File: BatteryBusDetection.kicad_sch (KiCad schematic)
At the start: 12 parts, among them U1 S-8209AAA-T8T1U, U2 S-8209AAA-T8T1U

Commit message: Refactored schematics and silkscreen
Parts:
- C1, C2, C3, C4: footprint (none) -> Capacitor_SMD:C_0603_1608Metric
- R1, R2, R4, R5, R6, R7: footprint (none) -> Resistor_SMD:R_0603_1608Metric
- U1, U2: footprint TSSOP8-E-PKG_FT008-A-P-SD-1.2_ABL -> Battery-Board:TSSOP8-E-PKG_FT008-A-P-SD-1.2_ABL
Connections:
- net CHARGE_ENABLE renamed CHARGE_EN
- net DISCHARGE_ENABLE renamed DISCHARGE_EN
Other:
- note added: "delay = 10MOhms * C_cdt"
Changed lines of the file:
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@@
 		)
 	)
-	(hierarchical_label "CHARGE_ENABLE"
-		(shape output)
-		(at 237.49 81.28 0)
-		(fields_autoplaced yes)
+	(text "delay = 10MOhms * C_cdt"
+		(exclude_from_sim no)
+		(at 116.078 132.588 0)
 		(effects
 			(font
 				(size 1.27 1.27)
 			)
+		)
+	)
+	(hierarchical_label "CHARGE_EN"
+		(shape output)
+		(at 237.49 81.28 0)
+		(fields_autoplaced yes)
+		(effects
+			(font
+				(size 1.27 1.27)
+			)
 			(justify left)
 		)
@@
 		)
 	)
-	(hierarchical_label "DISCHARGE_ENABLE"
+	(hierarchical_label "DISCHARGE_EN"
 		(shape output)
 		(at 237.49 83.82 0)
@@
 			)
 		)
-		(property "Footprint" ""
+		(property "Footprint" "Resistor_SMD:R_0603_1608Metric"
 			(at 161.29 102.87 0)
 			(effects
@@
 			)
 		)
-		(property "Footprint" ""
+		(property "Footprint" "Resistor_SMD:R_0603_1608Metric"
 			(at 102.87 105.41 0)
 			(effects
@@
 			)
 		)
-		(property "Footprint" ""
+		(property "Footprint" "Capacitor_SMD:C_0603_1608Metric"
 			(at 102.87 124.46 0)
 			(effects
@@
 			)
 		)
-		(property "Footprint" ""
+		(property "Footprint" "Resistor_SMD:R_0603_1608Metric"
 			(at 92.71 124.46 0)
 			(effects
@@
 			)
 		)
-		(property "Footprint" "TSSOP8-E-PKG_FT008-A-P-SD-1.2_ABL"
+		(property "Footprint" "Battery-Board:TSSOP8-E-PKG_FT008-A-P-SD-1.2_ABL"
 			(at 116.84 111.76 0)
 			(effects
@@
 			)
 		)
-		(property "Footprint" ""
+		(property "Footprint" "Capacitor_SMD:C_0603_1608Metric"
 			(at 182.88 91.44 0)
 			(effects
@@
 			)
 		)
-		(property "Footprint" ""
+		(property "Footprint" "Resistor_SMD:R_0603_1608Metric"
 			(at 171.45 69.85 0)
 			(effects
@@
 			)
 		)
-		(property "Footprint" ""
+		(property "Footprint" "Capacitor_SMD:C_0603_1608Metric"
 			(at 171.45 91.44 0)
 			(effects
@@
 			)
 		)
-		(property "Footprint" ""
+		(property "Footprint" "Capacitor_SMD:C_0603_1608Metric"
 			(at 114.3 124.46 0)
 			(effects
@@
 			)
 		)
-		(property "Footprint" ""
+		(property "Footprint" "Resistor_SMD:R_0603_1608Metric"
 			(at 167.64 111.76 0)
 			(effects
@@
 			)
 		)
-		(property "Footprint" "TSSOP8-E-PKG_FT008-A-P-SD-1.2_ABL"
+		(property "Footprint" "Battery-Board:TSSOP8-E-PKG_FT008-A-P-SD-1.2_ABL"
 			(at 185.42 78.74 0)
 			(effects
@@
 			)
 		)
-		(property "Footprint" ""
+		(property "Footprint" "Resistor_SMD:R_0603_1608Metric"
 			(at 83.82 124.46 0)
 			(effects

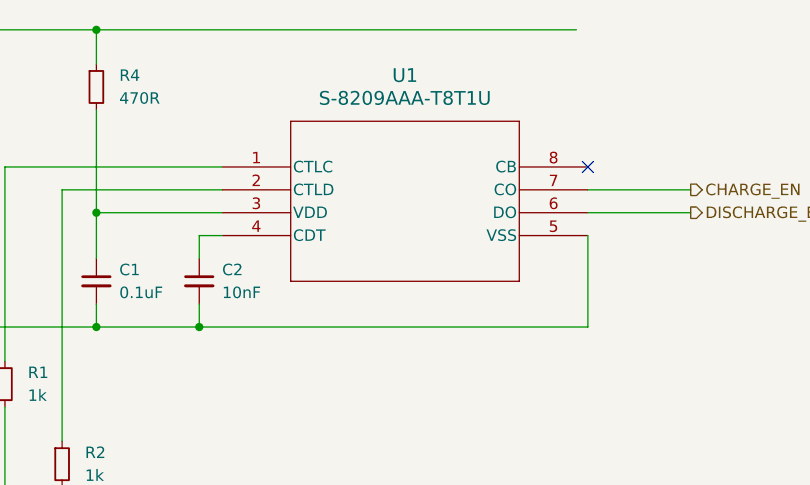
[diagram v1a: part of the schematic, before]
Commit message: Changes for lib refactor
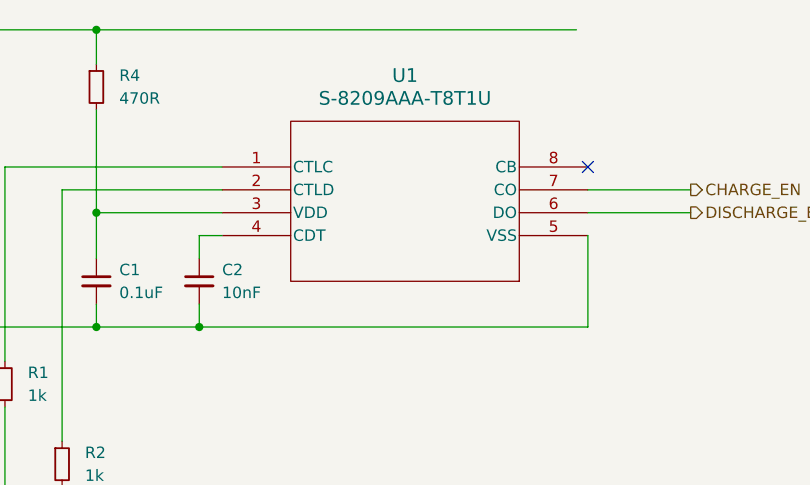
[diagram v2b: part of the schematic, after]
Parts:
- U1, U2: footprint Battery-Board:TSSOP8-E-PKG_FT008-A-P-SD-1.2_ABL -> Argus-IC:TSSOP8-E-PKG_FT008-A-P-SD-1.2_ABL; symbol Battery-Board:S-8209AAA-T8T1U -> Argus-IC:S-8209AAA-T8T1U
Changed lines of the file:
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@@
 	)
 	(symbol
-		(lib_name "S-8209AAA-T8T1U_1")
-		(lib_id "Battery-Board:S-8209AAA-T8T1U")
+		(lib_id "Argus-IC:S-8209AAA-T8T1U")
 		(at 116.84 111.76 0)
 		(unit 1)
@@
 			)
 		)
-		(property "Footprint" "Battery-Board:TSSOP8-E-PKG_FT008-A-P-SD-1.2_ABL"
+		(property "Footprint" "Argus-IC:TSSOP8-E-PKG_FT008-A-P-SD-1.2_ABL"
 			(at 116.84 111.76 0)
 			(effects
@@
 	)
 	(symbol
-		(lib_id "Battery-Board:S-8209AAA-T8T1U")
+		(lib_id "Argus-IC:S-8209AAA-T8T1U")
 		(at 185.42 78.74 0)
 		(unit 1)
@@
 			)
 		)
-		(property "Footprint" "Battery-Board:TSSOP8-E-PKG_FT008-A-P-SD-1.2_ABL"
+		(property "Footprint" "Argus-IC:TSSOP8-E-PKG_FT008-A-P-SD-1.2_ABL"
 			(at 185.42 78.74 0)
 			(effects

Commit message: Fixes from feedback
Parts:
- U1, U2: footprint Argus-IC:TSSOP8-E-PKG_FT008-A-P-SD-1.2_ABL -> TSSOP8-E-PKG_FT008-A-P-SD-1.2_ABL
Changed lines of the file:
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@@
 			)
 		)
-		(property "Footprint" "Argus-IC:TSSOP8-E-PKG_FT008-A-P-SD-1.2_ABL"
+		(property "Footprint" "TSSOP8-E-PKG_FT008-A-P-SD-1.2_ABL"
 			(at 116.84 111.76 0)
 			(effects
@@
 			)
 		)
-		(property "Footprint" "Argus-IC:TSSOP8-E-PKG_FT008-A-P-SD-1.2_ABL"
+		(property "Footprint" "TSSOP8-E-PKG_FT008-A-P-SD-1.2_ABL"
 			(at 185.42 78.74 0)
 			(effects

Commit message: v2.1 (v3?) Partial Updates
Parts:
- U1: renamed from U2; footprint TSSOP8-E-PKG_FT008-A-P-SD-1.2_ABL -> Argus-IC:TSSOP8-E-PKG_FT008-A-P-SD-1.2_ABL
- U2: renamed from U1; footprint TSSOP8-E-PKG_FT008-A-P-SD-1.2_ABL -> Argus-IC:TSSOP8-E-PKG_FT008-A-P-SD-1.2_ABL
- renumbered C3 to C1, C4 to C2, C1 to C3, C2 to C4, R7 to R1, R6 to R2, R5 to R3, R1 to R4, R2 to R5, R4 to R6
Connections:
- net BATT0 renamed BATT_N
- net BATT1 renamed BATT_M
- net BATT2 renamed BATT_P
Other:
- note added: "Battery protection design derived from Portland State University's Open-Source OreSat project"
- note added: "S-8209A has a Vov = 4.100V (release = 4.000V) and a Vuv = 2.500V (release = 2.700V)"
- note added: "t_D = 10.0 MΩ typ. × C_CDT [μF] t_D = 0.1s"
- note removed: "delay = 10MOhms * C_cdt"
- company: (none) -> Carnegie Mellon University
- title: (none) -> Argus Batteryboard
- moved on the sheet: C1, C2, C3, C4, R1, R2, R3, R4, R5, R6, U1, U2

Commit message: v3.1 Updates
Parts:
- C1, C3: value 0.1uF -> 100n
- C2, C4: value 10nF -> 10n
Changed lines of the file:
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@@
 		(dnp no)
 		(property "Reference" "C1"
-			(at 88.646 124.714 0)
-			(effects
-				(font
-					(size 1.27 1.27)
-				)
-				(justify left)
-			)
-		)
-		(property "Value" "0.1uF"
-			(at 88.646 126.746 0)
+			(at 88.392 124.714 0)
+			(effects
+				(font
+					(size 1.27 1.27)
+				)
+				(justify left)
+			)
+		)
+		(property "Value" "100n"
+			(at 88.392 126.746 0)
 			(effects
 				(font
@@
 		(dnp no)
 		(property "Reference" "C4"
-			(at 167.386 91.694 0)
-			(effects
-				(font
-					(size 1.27 1.27)
-				)
-				(justify left)
-			)
-		)
-		(property "Value" "10nF"
-			(at 167.386 93.726 0)
+			(at 167.132 91.694 0)
+			(effects
+				(font
+					(size 1.27 1.27)
+				)
+				(justify left)
+			)
+		)
+		(property "Value" "10n"
+			(at 167.132 93.726 0)
 			(effects
 				(font
@@
 		(dnp no)
 		(property "Reference" "C3"
-			(at 157.226 91.694 0)
-			(effects
-				(font
-					(size 1.27 1.27)
-				)
-				(justify left)
-			)
-		)
-		(property "Value" "0.1uF"
-			(at 157.226 93.726 0)
+			(at 156.972 91.694 0)
+			(effects
+				(font
+					(size 1.27 1.27)
+				)
+				(justify left)
+			)
+		)
+		(property "Value" "100n"
+			(at 156.972 93.726 0)
 			(effects
 				(font
@@
 		(dnp no)
 		(property "Reference" "C2"
-			(at 98.806 124.714 0)
-			(effects
-				(font
-					(size 1.27 1.27)
-				)
-				(justify left)
-			)
-		)
-		(property "Value" "10nF"
-			(at 98.806 126.746 0)
-			(effects
-				(font
+			(at 98.552 124.714 0)
+			(effects
+				(font
+					(size 1.27 1.27)
+				)
+				(justify left)
+			)
+		)
+		(property "Value" "10n"
+			(at 98.552 126.746 0)
+			(effects
+				(font

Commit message: Idk some changes
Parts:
- C1, C3: MPN (none) -> C307348
- C2, C4: MPN (none) -> C161232
- R1, R2, R4, R5: MPN (none) -> C2484712
- R3, R6: MPN (none) -> C844564
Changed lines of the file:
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@@
+			)
+		)
+		(property "MPN" "C2484712"
+			(at 142.24 92.71 0)
+			(effects
+				(font
+					(size 1.27 1.27)
+				)
+				(hide yes)
 			)
 		)
@@
 			)
 		)
+		(property "MPN" "C844564"
+			(at 86.36 106.68 0)
+			(effects
+				(font
+					(size 1.27 1.27)
+				)
+				(hide yes)
+			)
+		)
 		(pin "2"
 		)
@@
 			)
 		)
+		(property "MPN" "C307348"
+			(at 86.36 125.73 0)
+			(effects
+				(font
+					(size 1.27 1.27)
+				)
+				(hide yes)
+			)
+		)
 		(pin "1"
 		)
@@
 			)
 		)
+		(property "MPN" "C2484712"
+			(at 80.01 125.73 0)
+			(effects
+				(font
+					(size 1.27 1.27)
+				)
+				(hide yes)
+			)
+		)
 		(pin "2"
 		)
@@
 			)
 		)
+		(property "MPN" "C161232"
+			(at 165.1 92.71 0)
+			(effects
+				(font
+					(size 1.27 1.27)
+				)
+				(hide yes)
+			)
+		)
 		(pin "1"
 		)
@@
 			)
 		)
+		(property "MPN" "C844564"
+			(at 154.94 71.12 0)
+			(effects
+				(font
+					(size 1.27 1.27)
+				)
+				(hide yes)
+			)
+		)
 		(pin "2"
 		)
@@
 			)
 		)
+		(property "MPN" "C307348"
+			(at 154.94 92.71 0)
+			(effects
+				(font
+					(size 1.27 1.27)
+				)
+				(hide yes)
+			)
+		)
 		(pin "1"
 		)
@@
 			)
 		)
+		(property "MPN" "C161232"
+			(at 96.52 125.73 0)
+			(effects
+				(font
+					(size 1.27 1.27)
+				)
+				(hide yes)
+			)
+		)
 		(pin "1"
 		)
@@
 			)
 		)
+		(property "MPN" "C2484712"
+			(at 148.59 92.71 0)
+			(effects
+				(font
+					(size 1.27 1.27)
+				)
+				(hide yes)
+			)
+		)
 		(pin "2"
 		)
@@
 			(at 73.66 125.73 0)
 			(effects
+				(font
+					(size 1.27 1.27)
+				)
+				(hide yes)
+			)
+		)
+		(property "MPN" "C2484712"
+			(at 73.66 125.73 0)
+			(effects
